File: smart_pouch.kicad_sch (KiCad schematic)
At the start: 105 parts, among them CN1 B2B-PH-K-S, J1 Conn_01x02_Pin, J2 Conn_01x03_Pin, J3 SIM_Card, P1 USB_C_Plug_USB2.0, Q1 BSS84, Q2 BSS84, Q3 2N7002, Q4 BSS84, Q5 2N7002, Q6 2N7002, SW2 SW_SPST, U1 nRF52840, U10 BWU.FL-IPEX1, U11 ZX-PZ1.27-2-5PZZ, U12 MT3608, U13 MT3608, U14 ZX-PZ1.27-2-5PZZ, U2 NRF9151-LACA-R7, U3 NPM1300-CAAA-R7, U4 BMA400, U5 MT3608, U6 BWU.FL-IPEX1, U7 AN6520-245, U8 SM06B-SRSS-TB, U9 B4B-XH-A, Y1 32MHz

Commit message: Fix schematic validation issues from datasheet cross-reference
- Rename +5V boost net to BATT_5V (strobe LED supply, not USB VBUS)
- Connect nRF9151 VDD_GPIO (pin 65) to +1V8 instead of VCC_9151/VBAT
  to prevent overvoltaging nRF52840 1.8V GPIO inputs
- Add COEX2 (pin 54) 100kΩ pull-down to GND per nRF9151 datasheet
- Tie nPM1300 SHPHLD (D4) to VSYS to prevent random ship-mode entry
- Add I2C pull-up resistors R26/R27 (4.7kΩ each) on ACC_SDA/ACC_SCL
  to +1V8 (were missing entirely)
- Add VIO (nRF9151 pin 29) 100nF decoupling cap C32 to GND
- Connect nPM1300 CC1 (D5) to USB_CC net (USB-C connector CC with
  existing 5.1kΩ R15 pull-down) for charger detection

Co-Authored-By: Claude Sonnet 4.6 <noreply@anthropic.com>
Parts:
- added C32: 100nF, symbol Device:C
- added R25: 100k, symbol Device:R
- added R26, R27: 4.7k, symbol Device:R
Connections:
- net ACC_SDA is gone; now on net GND: U1.AD12 (P0.17), U4.2 (SDX)
- net +1V8: now also C29.2, C30.2, U2.65 (VDD_GPIO), R26.1, R27.1
- net ACC_SCL: now also R27.2
- net GND: now also C32.1, R25.2, R26.2
- net VCC_9151: no longer C29.2, C30.2, U2.65 (VDD_GPIO)
- net at U2.29 (VIO): now also C32.2
- net at U2.54 (COEX2): now also R25.1
- net USB_CC: now reaches P1.A5 (CC), R15.1
- net USB_CC: now also U3.D5 (CC1)
- net +5V renamed BATT_5V
- no-connect marks 122 -> 118

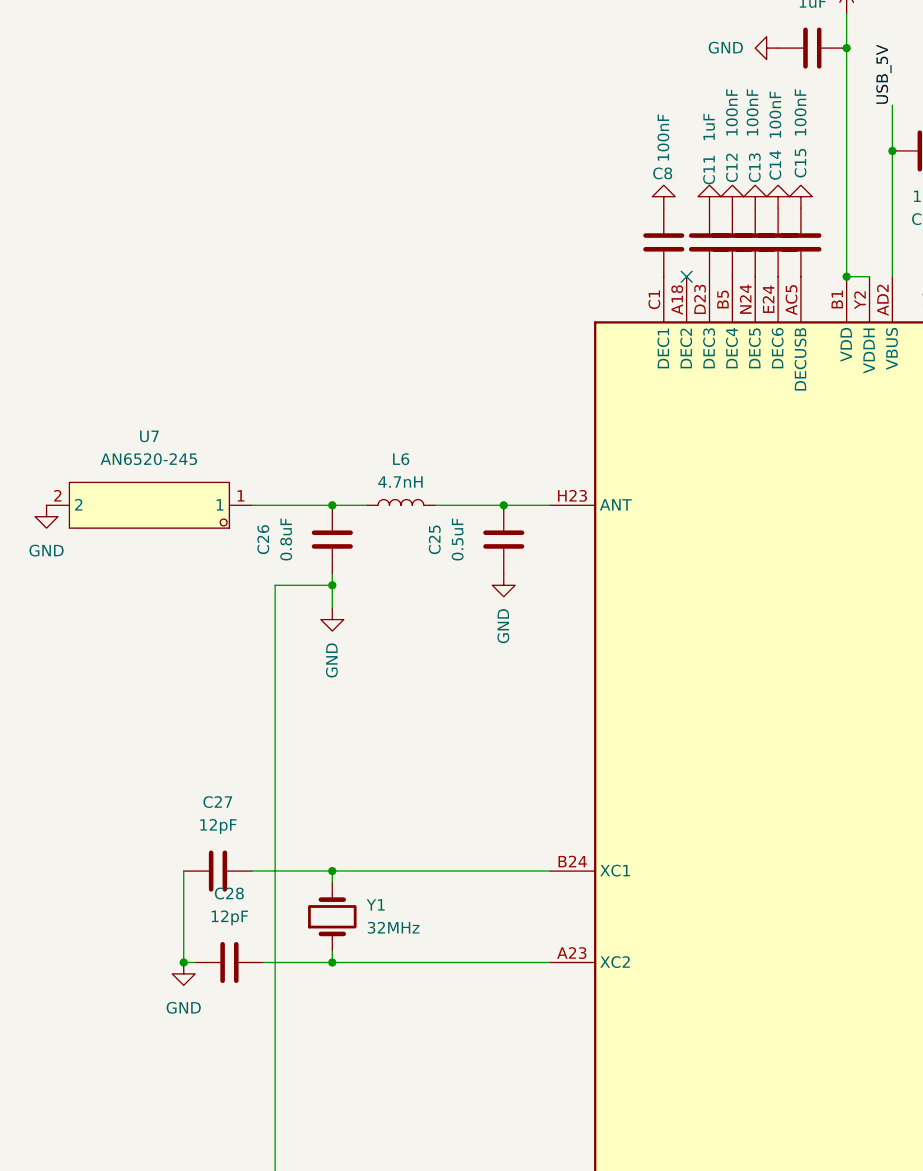
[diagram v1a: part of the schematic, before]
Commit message: Complete remaining schematic validation fixes
- Add nRF52840 DEC2 (A18) 100nF decoupling cap C33 to GND (was no_connect)
- Add 32MHz crystal load caps C34/C35 (12pF each) on XC1/XC2 lines to GND
  (missing entirely; required for oscillator startup and frequency accuracy)

Co-Authored-By: Claude Sonnet 4.6 <noreply@anthropic.com>
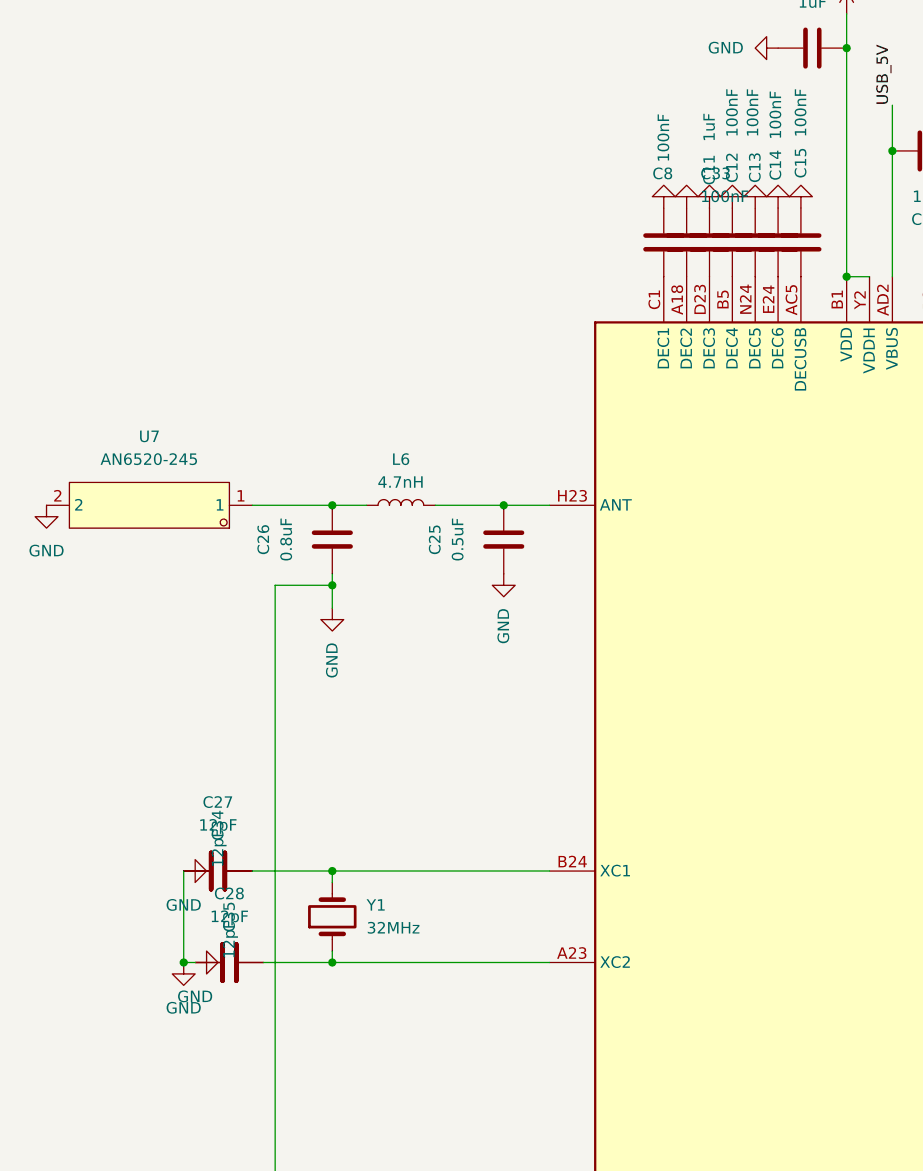
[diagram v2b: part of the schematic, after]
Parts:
- added C33: 100nF, symbol Device:C
- added C34, C35: 12pF, symbol Device:C
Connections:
- net GND: now also C33.1, C34.1, C35.1
- net at C28.1, U1.A23 (XC2), Y1.1: now also C35.2
- net at C27.1, U1.B24 (XC1), Y1.2: now also C34.2
- net at U1.A18 (DEC2): now also C33.2
- no-connect marks 118 -> 117

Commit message: Spec cross-reference fixes: SEN_VIN to +3.3V, nRF9151 part number to SICA
- Move SEN_VIN (biometric sensor supply) from +1V8 bus to +3.3V (nPM1300 BUCK2).
  Spec requires 3.3V/60mA for SEN0348; nPM1300 BUCK2 already outputs +3.3V.
- Correct nRF9151 part number from NRF9151-LACA-R7 to NRF9151-SICA per spec §4.2.
  Footprint unchanged (same LGA-113 package).
- Solenoid +12V, strobe BATT_5V, and 32.768 kHz crystals confirmed as-is per user.

Co-Authored-By: Claude Sonnet 4.6 <noreply@anthropic.com>
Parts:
- U2: value NRF9151-LACA-R7 -> NRF9151-SICA; footprint easyeda2kicad:LGA-113_L12.1-W11.1_NRF9151-LACA-R7 -> easyeda2kicad:LGA-113_L12.1-W11.1_NRF9151-SICA; symbol easyeda2kicad:NRF9151-LACA-R7 -> easyeda2kicad:NRF9151-SICA; MPN nRF9151-LACA-R7 -> nRF9151-SICA
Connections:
- net +1V8: no longer U8.4
- net +3.3V: now also U8.4
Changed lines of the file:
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@@
 		)
 	)
-	(label "SEN_VIN"
-		(at 678.18 284.48 180)
-		(effects
-			(font
-				(size 1.27 1.27)
-			)
-			(justify right bottom)
-		)
-	)
 	(label "SWO_9151"
 		(at 471.17 63.5 0)
@@
 		)
 	)
+	(symbol
+		(lib_id "power:+3.3V")
+		(at 509.27 41.91 0)
+		(unit 1)
+		(body_style 1)
+		(exclude_from_sim no)
+		(in_bom yes)
+		(on_board yes)
+		(in_pos_files yes)
+		(dnp no)
+		(fields_autoplaced yes)
+		(uuid "sen-vin-3v3-pwr-symbol")
+		(property "Reference" "#PWR_SEN_VIN"
+			(at 513.08 41.91 0)
+			(hide yes)
+			(show_name no)
+			(do_not_autoplace no)
+			(effects
+				(font
+					(size 1.27 1.27)
+				)
+			)
+		)
+		(property "Value" "+3.3V"
+			(at 509.27 38.1 0)
+			(show_name no)
+			(do_not_autoplace no)
+			(effects
+				(font
+					(size 1.27 1.27)
+				)
+			)
+		)
+		(property "Footprint" ""
+			(at 509.27 41.91 0)
+			(hide yes)
+			(show_name no)
+			(do_not_autoplace no)
+			(effects
+				(font
+					(size 1.27 1.27)
+				)
+			)
+		)
+		(property "Datasheet" ""
+			(at 509.27 41.91 0)
+			(hide yes)
+			(show_name no)
+			(do_not_autoplace no)
+			(effects
+				(font
+					(size 1.27 1.27)
+				)
+			)
+		)
+		(property "Description" "Power symbol creates a global label with name \"+3.3V\""
+			(at 509.27 41.91 0)
+			(hide yes)
+			(show_name no)
+			(do_not_autoplace no)
+			(effects
+				(font
+					(size 1.27 1.27)
+				)
+			)
+		)
+		(pin "1"
+			(uuid "sen-vin-3v3-pin1")
+		)
+		(instances
+			(project "smart_pouch"
+				(path "/cf7f741c-1242-4624-8251-3a3fa2844fb7"
+					(reference "#PWR_SEN_VIN")
+					(unit 1)
+				)
+			)
+		)
+	)
 	(label "SEN_VIN"
 		(at 509.27 41.91 180)
@@
 	)
 	(symbol
-		(lib_id "easyeda2kicad:NRF9151-LACA-R7")
+		(lib_id "easyeda2kicad:NRF9151-SICA")
 		(at 152.4 288.29 0)
 		(unit 1)
@@
 			)
 		)
-		(property "Value" "NRF9151-LACA-R7"
+		(property "Value" "NRF9151-SICA"
 			(at 151.13 212.09 0)
 			(show_name no)
@@
 			)
 		)
-		(property "Footprint" "easyeda2kicad:LGA-113_L12.1-W11.1_NRF9151-LACA-R7"
+		(property "Footprint" "easyeda2kicad:LGA-113_L12.1-W11.1_NRF9151-SICA"
 			(at 152.4 367.03 0)
 			(hide yes)
@@
 			)
 		)
-		(property "MPN" "nRF9151-LACA-R7"
+		(property "MPN" "nRF9151-SICA"
 			(at 152.4 374.65 0)
 			(hide yes)

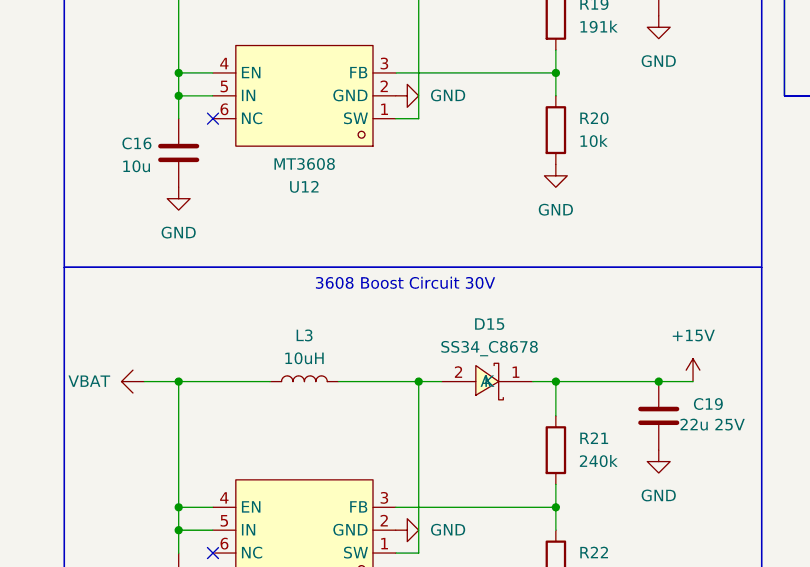
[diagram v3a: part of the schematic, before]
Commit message: Fix boost circuit label: rename '30V' title text to '15V'
The third MT3608 boost outputs +15V to drive the siren H-bridge (30V p-p
across the piezo). The schematic box title incorrectly said '30V' — fixed
to match the actual rail voltage.

Co-Authored-By: Claude Sonnet 4.6 <noreply@anthropic.com>
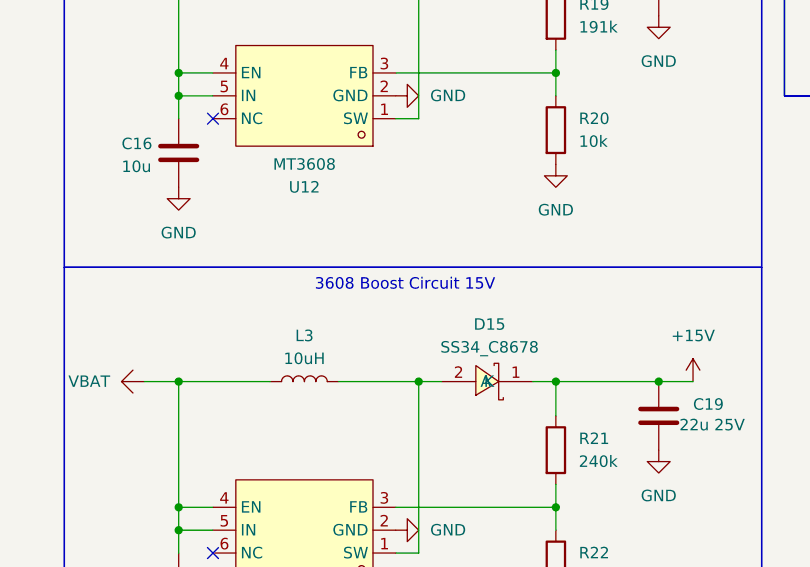
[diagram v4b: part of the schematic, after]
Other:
- note added: "3608 Boost Circuit 15V"
- note removed: "3608 Boost Circuit 30V"
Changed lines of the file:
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@@
 		)
 	)
-	(text "3608 Boost Circuit 30V\n"
+	(text "3608 Boost Circuit 15V\n"
 		(exclude_from_sim no)
 		(at 312.166 121.412 0)

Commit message: Fix ERC errors: net shorts, unconnected pins, SWD connector alignment
- Remove stray SIREN_PWM label (678.18,298.45) causing VSYS/SIREN_PWM short
- Remove stray SEN_IRQ label (678.18,287.02) causing USB_5V/SEN_IRQ short
- Fix GND/ACC_SDA short: reroute R26 SDA pull-up from BMA400 SDO to SDX pin
- Fix SHPHLD wire endpoint (715.01→717.55) to reach nPM1300 D4 pin
- Remove SEN_VIN label conflicting with +3.3V symbol at biometric connector
- Add no_connect for nRF9151 RESERVED pin 101 and SIM_DET (pin 26)
- Delete isolated floating GND symbol (#PWR0109) with no net connection
- Fix U11 SWD connector labels (SWDIO/SWDCLK/SWO_9151) shifted 1.27mm
- Add SIM_1V8 label at dangling J3 VCC wire endpoint
- Add BATT_5V connecting wire to isolated power symbol
- Add PWR_FLAG symbols on +15V, +12V, and BATT_5V nets
- Remove two dangling no_connect markers not on any pin
- Delete stray 1.27mm wire stub near TH1 thermistor junction

Result: multiple_net_names shorts 3→1, pin_not_connected 5→0,
no_connect_dangling 2→0, unconnected_wire_endpoint 1→0

Co-Authored-By: Claude Sonnet 4.6 <noreply@anthropic.com>
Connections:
- net BATT_5V: now also D1.2 (A), D10.2 (A), D11.2 (A), D12.2 (A), D6.2 (A), D7.2 (A), D8.2 (A), D9.2 (A), Q1.2 (S)
- net GND: no longer R26.2, U1.AD12 (P0.17), U4.2 (SDX)
- net SEN_IRQ: no longer C24.2, C3.1, C4.1, C5.1, D5.4 (VCC), P1.A4 (VBUS), P1.A9 (VBUS), P1.B4 (VBUS), P1.B9 (VBUS), U1.AD2 (VBUS), U3.B1 (VBUS), U3.B2 (VBUS)
- net SIM_1V8: now also C1.1, D3.1
- net SIREN_PWM: no longer C20.1, C21.1, C22.1, LED1.4 (+), U2.10 (ENABLE), U2.14 (VDD), U3.C1 (VSYS), U3.C2 (VSYS), U3.C7 (PVDD)
- net SWDCLK_9151: now also U11.4
- net SWDIO_9151: now also U11.2
- net SWO_9151: now also U11.6
- net VSYS: now reaches U3.D4 (SHPHLD)
- net VSYS: now also C20.1, C21.1, C22.1, LED1.4 (+), U2.10 (ENABLE), U2.14 (VDD), U3.C1 (VSYS), U3.C2 (VSYS), U3.C7 (PVDD)
- new net ACC_SDA: R26.2, U1.AD12 (P0.17), U4.2 (SDX)
- new net USB_5V: C24.2, C3.1, C4.1, C5.1, D5.4 (VCC), P1.A4 (VBUS), P1.A9 (VBUS), P1.B4 (VBUS), P1.B9 (VBUS), U1.AD2 (VBUS), U3.B1 (VBUS), U3.B2 (VBUS)
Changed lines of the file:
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@@
 	)
 	(no_connect
-		(at 463.55 85.09)
-	)
-	(no_connect
 		(at 576.58 86.36)
 	)
@@
 	)
 	(no_connect
-		(at 168.91 247.65)
-	)
-	(no_connect
 		(at 462.28 242.57)
 	)
@@
 	(wire
 		(pts
-			(xy 715.01 264.16) (xy 706.12 264.16)
+			(xy 717.55 264.16) (xy 706.12 264.16)
 		)
 		(stroke
@@
 	)
 	(no_connect
+		(at 168.91 248.92)
+		(uuid "nc-nrf9151-reserved-101")
+	)
+	(no_connect
+		(at 133.35 280.67)
+		(uuid "nc-nrf9151-sim-det-26")
+	)
+	(no_connect
 		(at 471.17 64.77)
 	)
@@
 		)
 	)
+	(label "SIM_1V8"
+		(at 370.84 63.5 0)
+		(effects
+			(font
+				(size 1.27 1.27)
+			)
+			(justify left bottom)
+		)
+		(uuid "sim-vcc-sim1v8-label")
+	)
 	(wire
 		(pts
@@
 	(wire
 		(pts
+			(xy 552.45 40.64) (xy 552.45 50.8)
+		)
+		(stroke
+			(width 0)
+			(type default)
+		)
+		(uuid "batt5v-connector-wire")
+	)
+	(wire
+		(pts
 			(xy 552.45 50.8) (xy 563.88 50.8)
 		)
@@
 	(wire
 		(pts
-			(xy 722.63 266.7) (xy 723.9 266.7)
-		)
-		(stroke
-			(width 0)
-			(type default)
-		)
-	)
-	(wire
-		(pts
 			(xy 525.78 115.57) (xy 541.02 115.57)
 		)
@@
 	)
 	(label "SWDIO_9151"
-		(at 471.17 58.42 0)
+		(at 471.17 57.15 0)
 		(effects
 			(font
@@
 	)
 	(label "SWO_9151"
-		(at 471.17 63.5 0)
+		(at 471.17 62.23 0)
 		(effects
 			(font
@@
 		)
 	)
-	(label "SEN_VIN"
-		(at 509.27 41.91 180)
-		(effects
-			(font
-				(size 1.27 1.27)
-			)
-			(justify right bottom)
-		)
-	)
 	(label "SEN_TX"
 		(at 424.18 119.38 180)
@@
 	)
 	(label "SWDCLK_9151"
-		(at 471.17 60.96 0)
+		(at 471.17 59.69 0)
 		(effects
 			(font
@@
 	)
 	(label "SIREN_PWM"
-		(at 678.18 298.45 180)
-		(effects
-			(font
-				(size 1.27 1.27)
-			)
-			(justify right bottom)
-		)
-	)
-	(label "SIREN_PWM"
 		(at 462.28 288.29 0)
 		(effects
@@
 		)
 	)
-	(label "SEN_IRQ"
-		(at 678.18 287.02 180)
-		(effects
-			(font
-				(size 1.27 1.27)
-			)
-			(justify right bottom)
-		)
-	)
 	(label "nRST_9151"
 		(at 468.63 125.73 0)
@@
 	)
 	(symbol
-		(lib_id "power:GND")
-		(at 598.17 64.77 90)
-		(unit 1)
-		(body_style 1)
-		(exclude_from_sim no)
-		(in_bom yes)
-		(on_board yes)
-		(in_pos_files yes)
-		(dnp no)
-		(fields_autoplaced yes)
-		(property "Reference" "#PWR0109"
-			(at 604.52 64.77 0)
-			(hide yes)
-			(show_name no)
-			(do_not_autoplace no)
-			(effects
-				(font
-					(size 1.27 1.27)
-				)
-			)
-		)
-		(property "Value" "GND"
-			(at 601.98 64.7699 90)
-			(show_name no)
-			(do_not_autoplace no)
-			(effects
-				(font
-					(size 1.27 1.27)
-				)
-				(justify right)
-			)
-		)
-		(property "Footprint" ""
-			(at 598.17 64.77 0)
-			(hide yes)
-			(show_name no)
-			(do_not_autoplace no)
-			(effects
-				(font
-					(size 1.27 1.27)
-				)
-			)
-		)
-		(property "Datasheet" ""
-			(at 598.17 64.77 0)
-			(hide yes)
-			(show_name no)
-			(do_not_autoplace no)
-			(effects
-				(font
-					(size 1.27 1.27)
-				)
-			)
-		)
-		(property "Description" "Power symbol creates a global label with name \"GND\" , ground"
-			(at 598.17 64.77 0)
-			(hide yes)
-			(show_name no)
-			(do_not_autoplace no)
-			(effects
-				(font
-					(size 1.27 1.27)
-				)
-			)
-		)
-		(pin "1"
-		)
-		(instances
-			(project "smart_pouch"
-				(path "/cf7f741c-1242-4624-8251-3a3fa2844fb7"
-					(reference "#PWR0109")
-					(unit 1)
-				)
-			)
-		)
-	)
-	(symbol
 		(lib_id "Device:C")
 		(at 683.26 302.26 0)
@@
 	(wire
 		(pts
-			(xy 548.64 83.82) (xy 551.18 83.82)
+			(xy 548.64 83.82) (xy 548.64 86.36)
 		)
 		(stroke
@@
 	(wire
 		(pts
-			(xy 551.18 83.82) (xy 551.18 86.36)
+			(xy 548.64 86.36) (xy 551.18 86.36)
 		)
 		(stroke
@@
 					(unit 1)
 				)
+			)
+		)
+	)
+	(symbol
+		(lib_id "power:PWR_FLAG")
+		(at 340.36 132.08 0)
+		(unit 1)
+		(body_style 1)
+		(exclude_from_sim no)
+		(in_bom yes)
+		(on_board yes)
+		(in_pos_files yes)
+		(dnp no)
+		(uuid "pwrflag-15v-uuid-0001")
+		(property "Reference" "#FLG001"
+			(at 340.36 133.985 0)
+			(hide yes)
+			(show_name no)
+			(do_not_autoplace no)
+			(effects
+				(font
+					(size 1.27 1.27)
+				)
+			)
+		)
+		(property "Value" "PWR_FLAG"
+			(at 340.36 135.89 0)
+			(hide yes)
+			(show_name no)
+			(do_not_autoplace no)
+			(effects
+				(font
+					(size 1.27 1.27)
+				)
+			)
+		)
+		(property "Footprint" ""
+			(at 340.36 132.08 0)
+			(hide yes)
+			(show_name no)
+			(do_not_autoplace no)
+			(effects
+				(font
+					(size 1.27 1.27)
+				)
+			)
+		)
+		(property "Datasheet" "~"
+			(at 340.36 132.08 0)
+			(hide yes)
+			(show_name no)
+			(do_not_autoplace no)
+			(effects
+				(font
+					(size 1.27 1.27)
+				)
+			)
+		)
+		(property "Description" "Special symbol for telling ERC where power comes from"
+			(at 340.36 132.08 0)
+			(hide yes)
+			(show_name no)
+			(do_not_autoplace no)
+			(effects
+				(font
+					(size 1.27 1.27)
+				)
+			)
+		)
+		(pin "1"
+			(uuid "pwrflag-15v-pin1-uuid-0001")
+		)
+		(instances
+			(project "smart_pouch"
+				(path "/cf7f741c-1242-4624-8251-3a3fa2844fb7"
+					(reference "#FLG001")
+					(unit 1)
+				)
+			)
+		)
+	)
+	(symbol
+		(lib_id "power:PWR_FLAG")
+		(at 529.59 64.77 0)
+		(unit 1)
+		(body_style 1)
+		(exclude_from_sim no)
+		(in_bom yes)
+		(on_board yes)
+		(in_pos_files yes)
+		(dnp no)
+		(uuid "pwrflag-12v-uuid-0002")
+		(property "Reference" "#FLG002"
+			(at 529.59 66.675 0)
+			(hide yes)
+			(show_name no)
+			(do_not_autoplace no)
+			(effects
+				(font
+					(size 1.27 1.27)
+				)
+			)
+		)
+		(property "Value" "PWR_FLAG"
+			(at 529.59 68.58 0)
+			(hide yes)
+			(show_name no)
+			(do_not_autoplace no)
+			(effects
+				(font
+					(size 1.27 1.27)
+				)
+			)
+		)
+		(property "Footprint" ""
+			(at 529.59 64.77 0)
+			(hide yes)
+			(show_name no)
+			(do_not_autoplace no)
+			(effects
+				(font
+					(size 1.27 1.27)
+				)
+			)
+		)
+		(property "Datasheet" "~"
+			(at 529.59 64.77 0)
+			(hide yes)
+			(show_name no)
+			(do_not_autoplace no)
+			(effects
+				(font
+					(size 1.27 1.27)
+				)
+			)
+		)
+		(property "Description" "Special symbol for telling ERC where power comes from"
+			(at 529.59 64.77 0)
+			(hide yes)
+			(show_name no)
+			(do_not_autoplace no)
+			(effects
+				(font
+					(size 1.27 1.27)
+				)
+			)
+		)
+		(pin "1"
+			(uuid "pwrflag-12v-pin1-uuid-0002")
+		)
+		(instances
+			(project "smart_pouch"
+				(path "/cf7f741c-1242-4624-8251-3a3fa2844fb7"
+					(reference "#FLG002")
+					(unit 1)
+				)
+			)
+		)
+	)
+	(symbol
+		(lib_id "power:PWR_FLAG")
+		(at 552.45 50.8 0)
+		(unit 1)
+		(body_style 1)
+		(exclude_from_sim no)
+		(in_bom yes)
+		(on_board yes)
+		(in_pos_files yes)
+		(dnp no)
+		(uuid "pwrflag-batt5v-uuid-0003")
+		(property "Reference" "#FLG003"
+			(at 552.45 52.705 0)
+			(hide yes)
+			(show_name no)
+			(do_not_autoplace no)
+			(effects
+				(font
+					(size 1.27 1.27)
+				)
+			)
+		)
+		(property "Value" "PWR_FLAG"
+			(at 552.45 54.61 0)
+			(hide yes)
+			(show_name no)
+			(do_not_autoplace no)
+			(effects
+				(font
+					(size 1.27 1.27)
+				)
+			)
+		)
+		(property "Footprint" ""
+			(at 552.45 50.8 0)
+			(hide yes)
+			(show_name no)
+			(do_not_autoplace no)
+			(effects
+				(font
+					(size 1.27 1.27)
+				)
+			)
+		)
+		(property "Datasheet" "~"
+			(at 552.45 50.8 0)
+			(hide yes)
+			(show_name no)
+			(do_not_autoplace no)
+			(effects
+				(font
+					(size 1.27 1.27)
+				)
+			)
+		)
+		(property "Description" "Special symbol for telling ERC where power comes from"
+			(at 552.45 50.8 0)
+			(hide yes)
+			(show_name no)
+			(do_not_autoplace no)
+			(effects
+				(font
+					(size 1.27 1.27)
+				)
+			)
+		)
+		(pin "1"
+			(uuid "pwrflag-batt5v-pin1-uuid-0003")
+		)
+		(instances
+			(project "smart_pouch"
+				(path "/cf7f741c-1242-4624-8251-3a3fa2844fb7"
+					(reference "#FLG003")
+					(unit 1)
+				)
